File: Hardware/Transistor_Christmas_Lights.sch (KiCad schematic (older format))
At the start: 5 parts, among them Q1 BC848

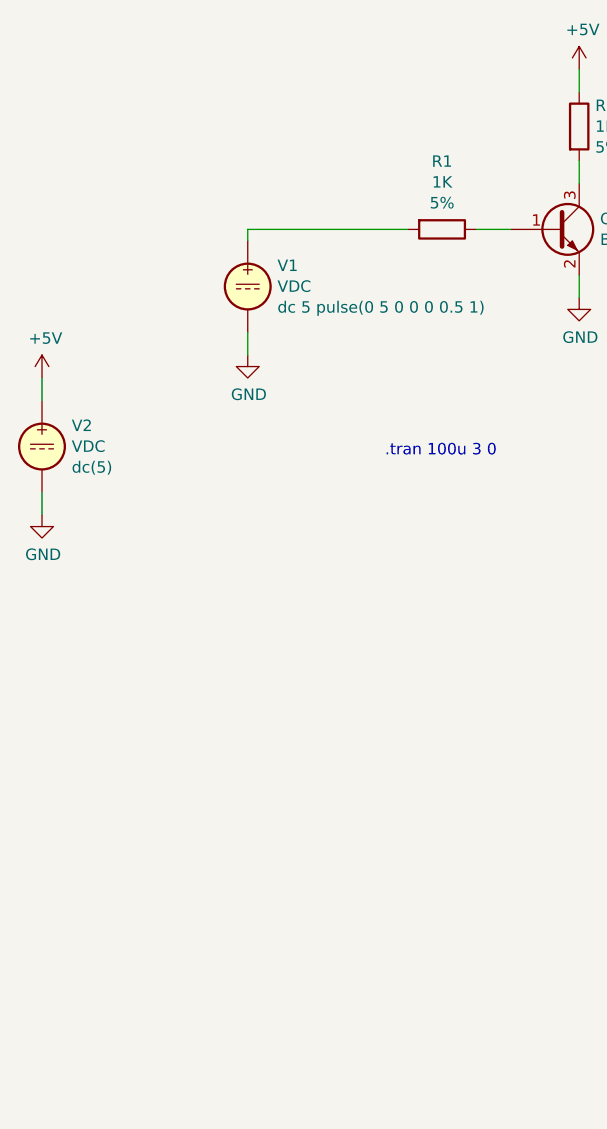
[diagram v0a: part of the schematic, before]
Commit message: Added led control logic to schematic. The second led power transistor will be added later.
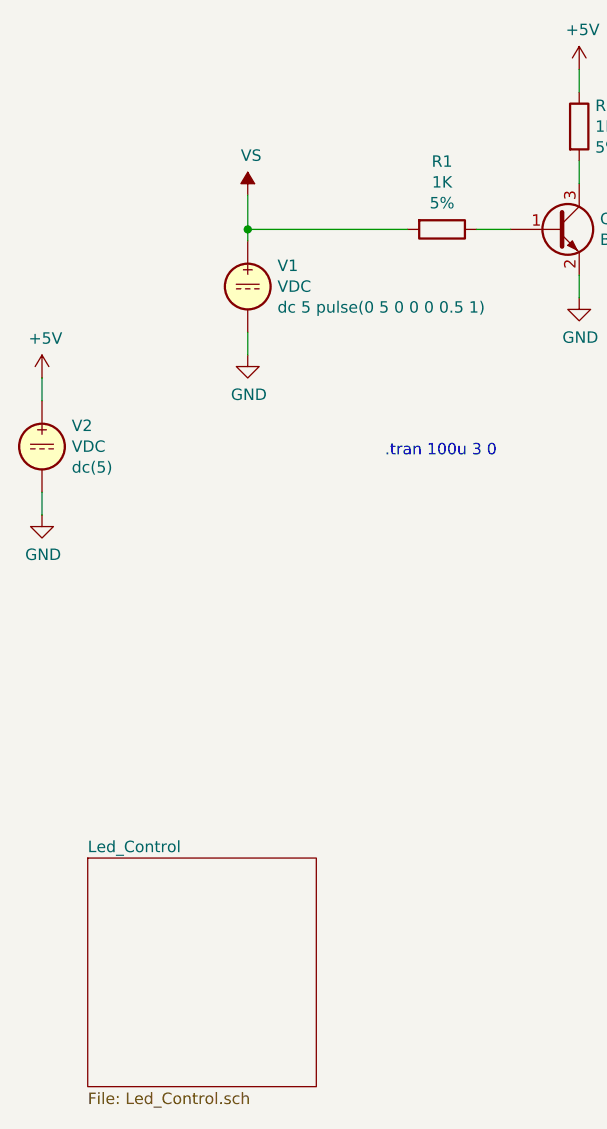
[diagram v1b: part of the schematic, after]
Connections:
- net VS: now reaches R1.2, V1.1
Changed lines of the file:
@@
 $Descr A4 11693 8268
 encoding utf-8
-Sheet 1 1
+Sheet 1 2
 Title "Main page"
 Date "2021-12-29"
@@
 Wire Wire Line
 	2200 2750 2900 2750
+$Sheet
+S 1500 5500 1000 1000
+U 61CE6682
+F0 "Led_Control" 50
+F1 "Led_Control.sch" 50
+$EndSheet
+Wire Wire Line
+	2200 2600 2200 2750
+Connection ~ 2200 2750
+$Comp
+L power:VS #PWR06
+U 1 1 61CE7722
+P 2200 2600
+F 0 "#PWR06" H 2000 2450 50  0001 C CNN
+F 1 "VS" H 2215 2773 50  0000 C CNN
+F 2 "" H 2200 2600 50  0001 C CNN
+F 3 "" H 2200 2600 50  0001 C CNN
+	1    2200 2600
+	1    0    0    -1
+$EndComp
 $EndSCHEMATC

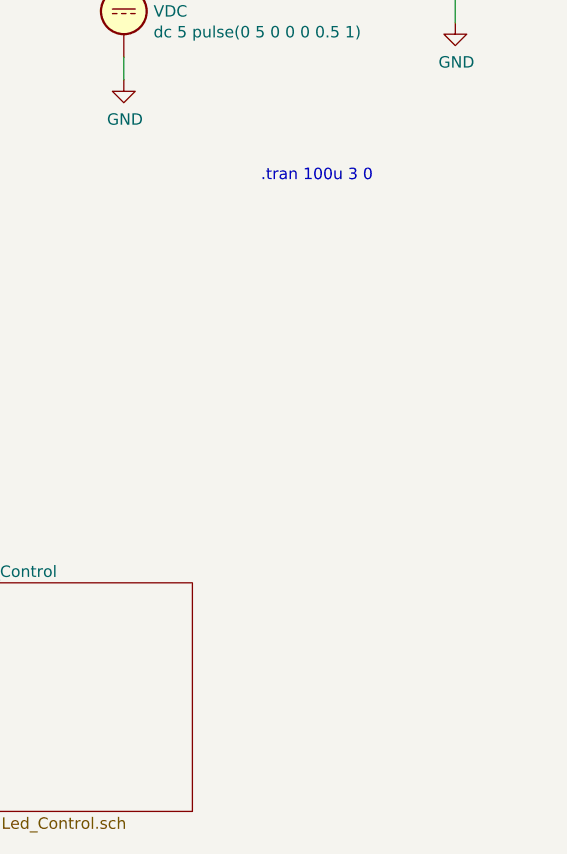
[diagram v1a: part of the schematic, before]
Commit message: Added the ring counter to the schematic.
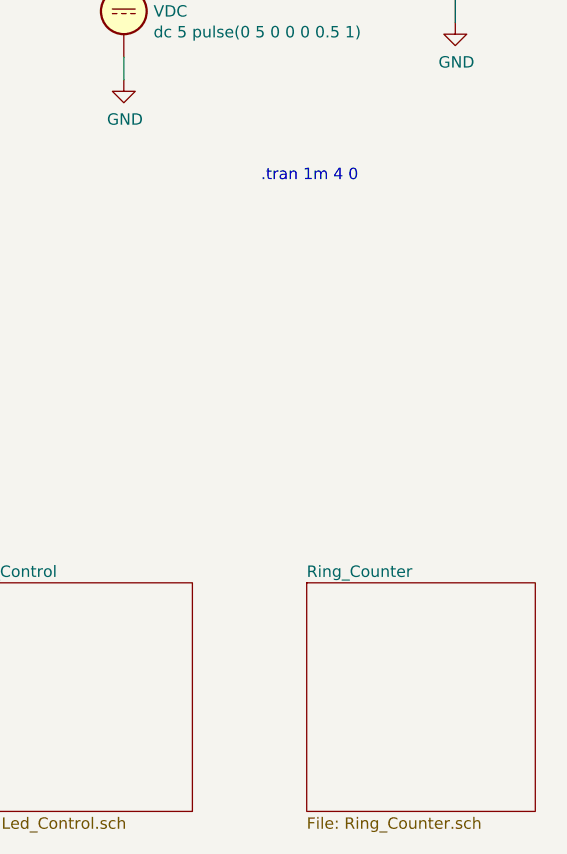
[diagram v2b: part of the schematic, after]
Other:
- note added: ".tran 1m 4 0"
- note removed: ".tran 100u 3 0"
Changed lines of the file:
@@
 $Descr A4 11693 8268
 encoding utf-8
-Sheet 1 2
+Sheet 1 3
 Title "Main page"
 Date "2021-12-29"
@@
 	2200 3200 2200 3300
 Text Notes 2800 3750 0    50   ~ 0
-.tran 100u 3 0
+.tran 1m 4 0
 Wire Wire Line
 	3650 2950 3650 3050
@@
 	1    0    0    -1
 $EndComp
+$Sheet
+S 3000 5500 1000 1000
+U 61D90E9A
+F0 "Ring_Counter" 50
+F1 "Ring_Counter.sch" 50
+$EndSheet
 $EndSCHEMATC

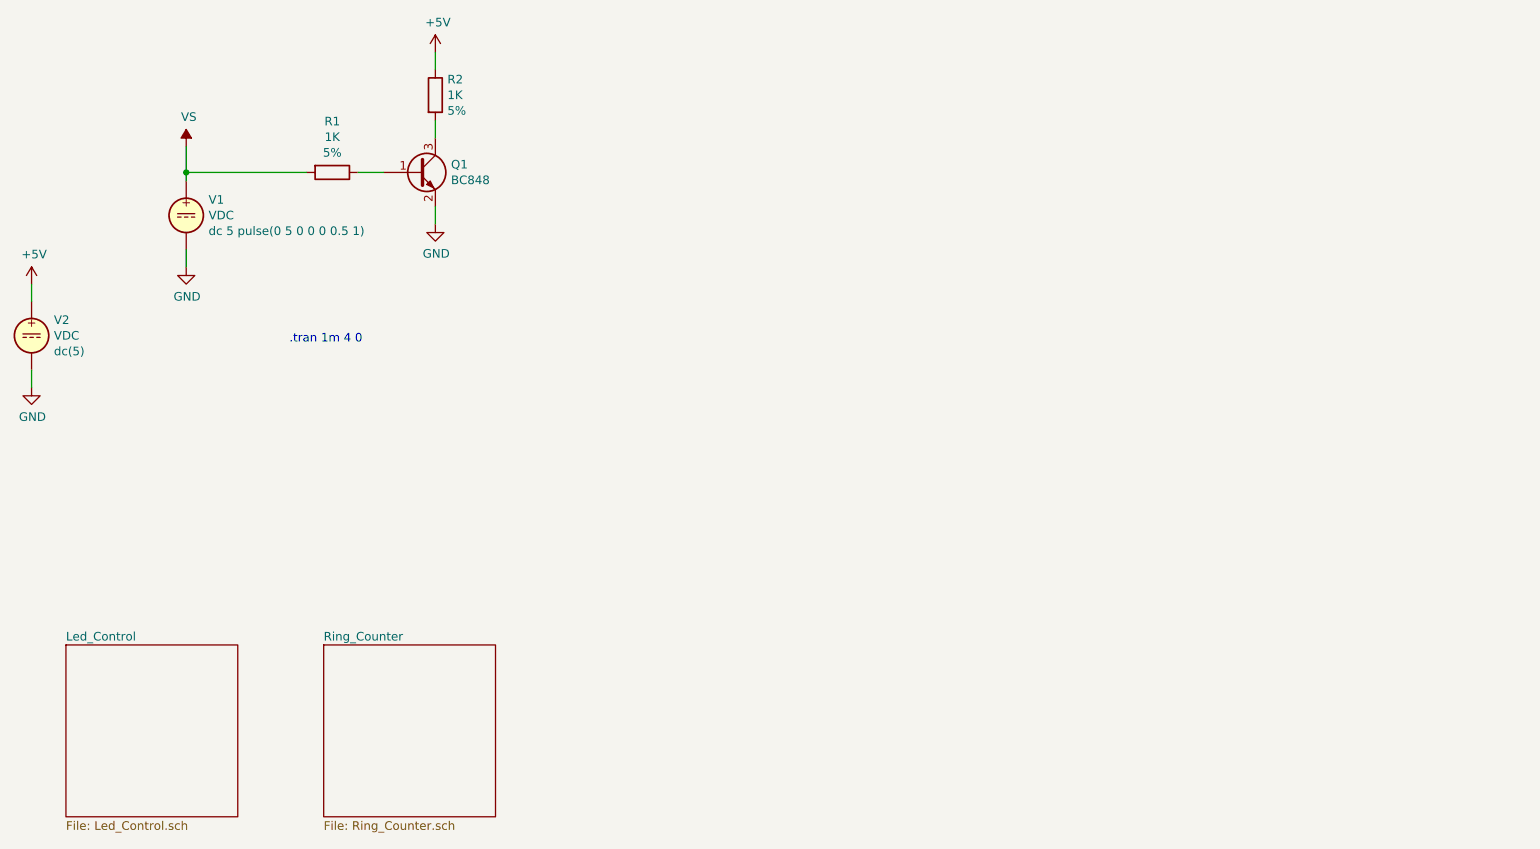
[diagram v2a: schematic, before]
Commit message: Improved ring counter RS latches output with better signal quality and less transistors count.
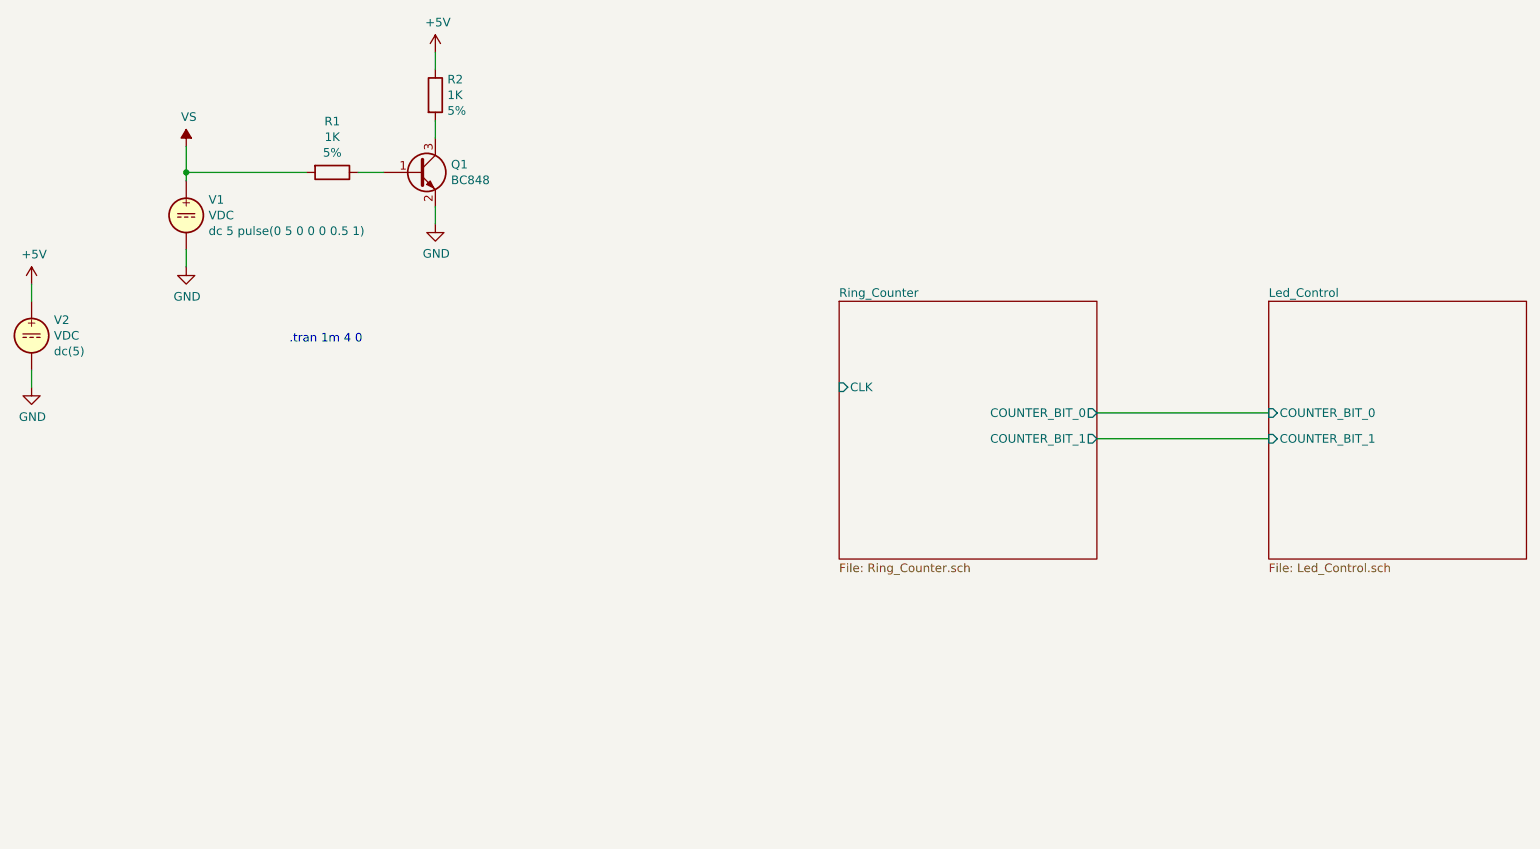
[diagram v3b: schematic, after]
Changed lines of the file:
@@
 	2200 2750 2900 2750
 $Sheet
-S 1500 5500 1000 1000
+S 8500 3500 1500 1500
 U 61CE6682
 F0 "Led_Control" 50
 F1 "Led_Control.sch" 50
+F2 "COUNTER_BIT_0" I L 8500 4150 50
+F3 "COUNTER_BIT_1" I L 8500 4300 50
 $EndSheet
 Wire Wire Line
@@
 $EndComp
 $Sheet
-S 3000 5500 1000 1000
+S 6000 3500 1500 1500
 U 61D90E9A
 F0 "Ring_Counter" 50
 F1 "Ring_Counter.sch" 50
+F2 "COUNTER_BIT_0" O R 7500 4150 50
+F3 "COUNTER_BIT_1" O R 7500 4300 50
+F4 "CLK" I L 6000 4000 50
 $EndSheet
+Wire Wire Line
+	7500 4150 8500 4150
+Wire Wire Line
+	8500 4300 7500 4300
 $EndSCHEMATC

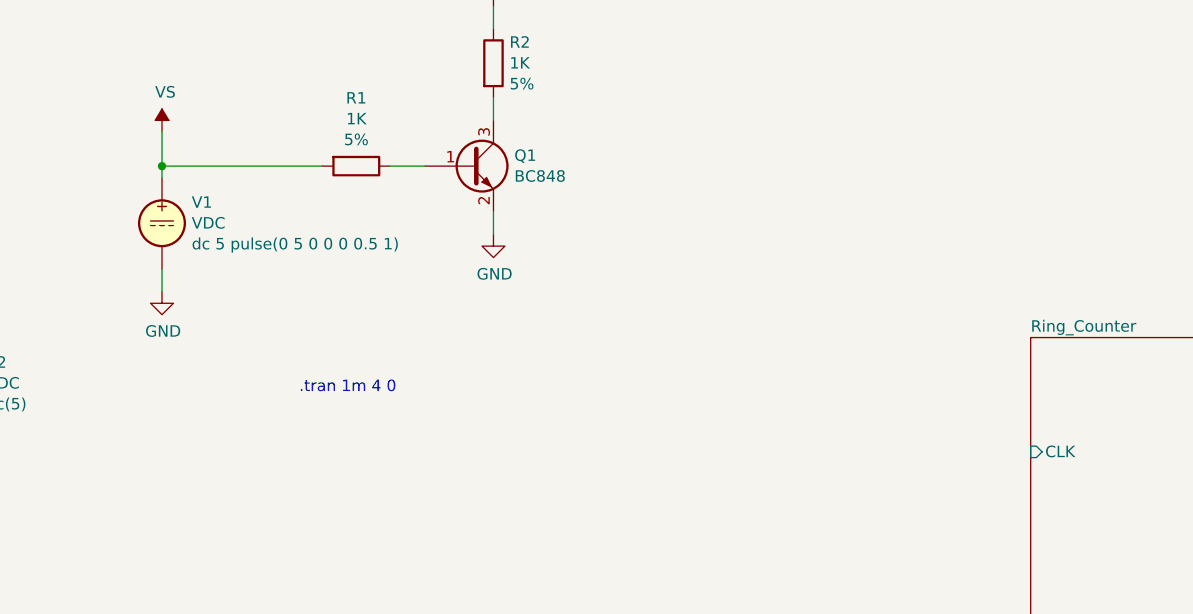
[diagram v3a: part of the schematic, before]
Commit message: Added second led logic and power transistor, also added BC858 SPICE model.
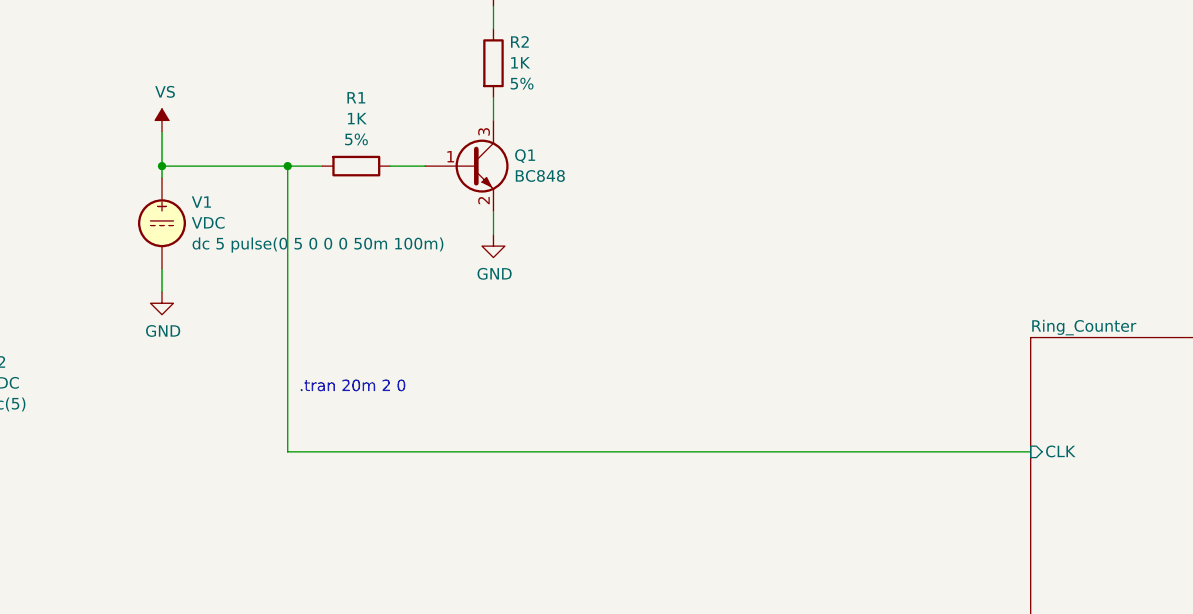
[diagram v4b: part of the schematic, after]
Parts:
- V1: Spice_Model dc 5 pulse(0 5 0 0 0 0.5 1) -> dc 5 pulse(0 5 0 0 0 50m 100m)
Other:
- note added: ".tran 20m 2 0"
- note removed: ".tran 1m 4 0"
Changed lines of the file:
@@
 F 4 "Y" H 2200 3000 50  0001 L CNN "Spice_Netlist_Enabled"
 F 5 "V" H 2200 3000 50  0001 L CNN "Spice_Primitive"
-F 6 "dc 5 pulse(0 5 0 0 0 0.5 1)" H 2330 2909 50  0000 L CNN "Spice_Model"
+F 6 "dc 5 pulse(0 5 0 0 0 50m 100m)" H 2330 2909 50  0000 L CNN "Spice_Model"
 	1    2200 3000
 	1    0    0    -1
@@
 	2200 3200 2200 3300
 Text Notes 2800 3750 0    50   ~ 0
-.tran 1m 4 0
+.tran 20m 2 0
 Wire Wire Line
 	3650 2950 3650 3050
@@
 	3650 2450 3650 2550
 Wire Wire Line
-	2200 2750 2900 2750
+	2200 2750 2750 2750
 $Sheet
 S 8500 3500 1500 1500
@@
 Wire Wire Line
 	8500 4300 7500 4300
+Wire Wire Line
+	2750 2750 2750 4000
+Wire Wire Line
+	2750 4000 6000 4000
+Connection ~ 2750 2750
+Wire Wire Line
+	2750 2750 2900 2750
 $EndSCHEMATC
